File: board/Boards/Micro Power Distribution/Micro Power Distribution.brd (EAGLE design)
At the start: 48.2 x 84.8 mm, 24 parts

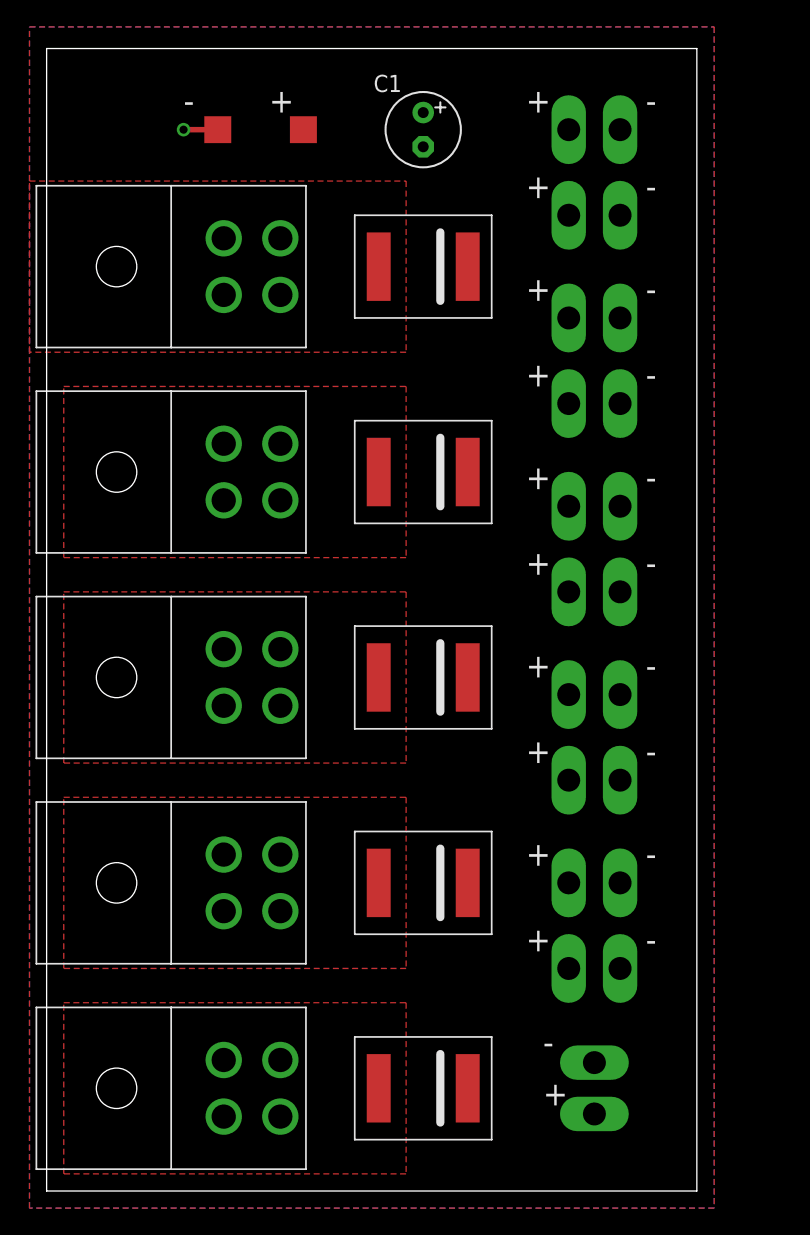
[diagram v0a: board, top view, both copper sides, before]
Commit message: updated power dist. board + created a micro version
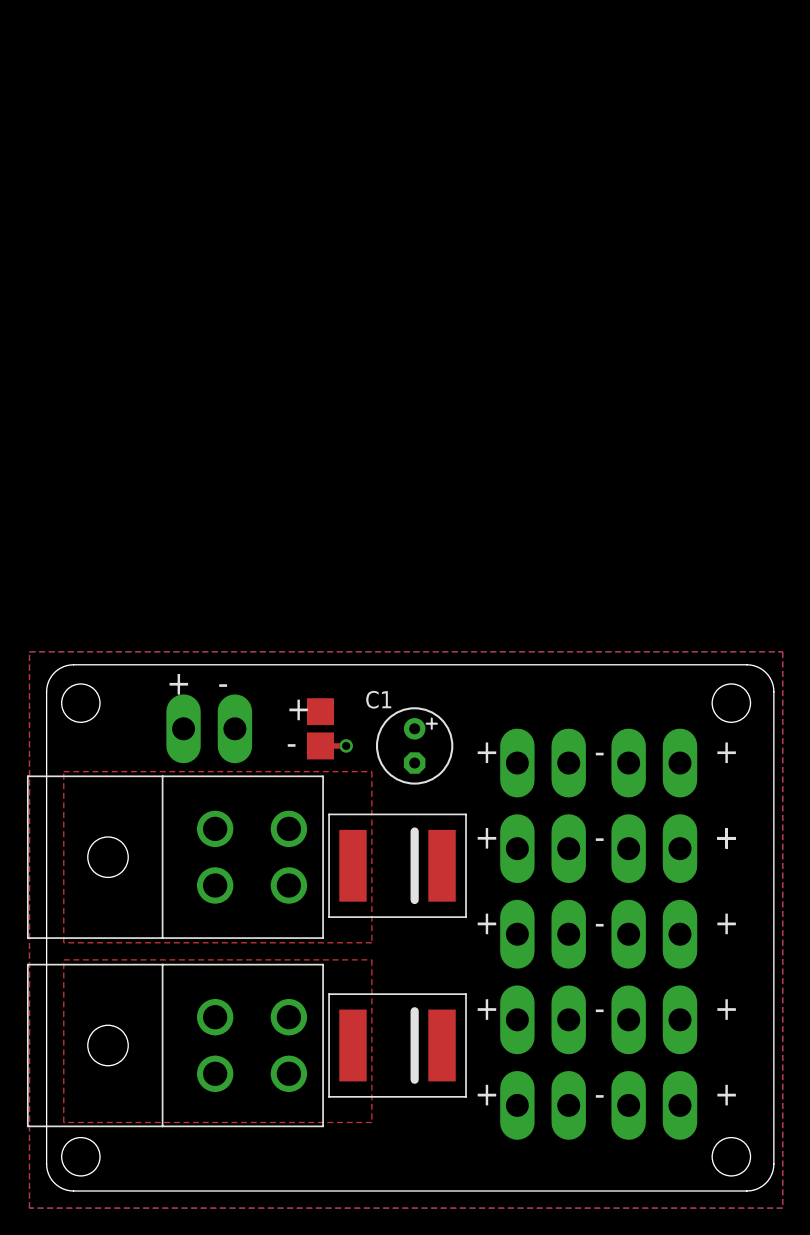
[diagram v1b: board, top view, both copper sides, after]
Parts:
- removed U$10, U$8, U$9: DO-214AB, Diodes:DO-214AB
- removed U$2, U$3, U$4: 2X2-MOLEX, Molex:2X2MOLEX
- moved TP4 53.5 mm to (45.1, 19.1), turned to 180 degrees
- moved TP8 47.2 mm to (45.1, 31.8), turned to 180 degrees
- moved TP13 46.4 mm to (20.3, 33.0)
- moved TP5 45.9 mm to (45.1, 12.7), turned to 180 degrees
- moved C1 45.7 mm to (27.3, 33.0)
- moved TP12 43.2 mm to (20.3, 35.6)
- moved TP6 38.4 mm to (45.1, 6.35), turned to 180 degrees
- moved TP9 33.2 mm to (36.8, 31.8)
- moved TP11 28.7 mm to (12.1, 34.3)
- moved TP10 25.8 mm to (45.1, 25.4), turned to 180 degrees
- moved TP7 6.35 mm to (36.8, 25.4)
- moved TP2 5.39 mm to (36.8, 12.7)
- moved TP3 5.39 mm to (36.8, 19.1)
- moved TP1 4.02 mm to (36.8, 6.35), turned to 0 degrees
- moved U$6 3.70 mm to (26.0, 10.8)
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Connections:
- removed net N$3: U$2.POWERL, U$2.POWERR, U$8.IN
- removed net N$4: U$3.POWERL, U$3.POWERR, U$9.IN
- removed net N$5: U$10.IN, U$4.POWERL, U$4.POWERR
- removed net N$6: C1.+, TP1.TP-1, TP10.TP-1, TP11.TP-1, TP12.TP, TP2.TP-1, TP3.TP-1, TP4.TP-1, TP5.TP-1, TP6.TP-1, TP7.TP-1, TP8.TP-1, TP9.TP-1, U$10.OUT, U$6.OUT, U$7.OUT, U$8.OUT, U$9.OUT
- new net N$10: C1.+, TP1.TP-1, TP10.TP-1, TP11.TP-1, TP12.TP, TP2.TP-1, TP3.TP-1, TP4.TP-1, TP5.TP-1, TP6.TP-1, TP7.TP-1, TP8.TP-1, TP9.TP-1, U$6.OUT, U$7.OUT
- net GND: no longer U$2.GNDL, U$2.GNDR, U$3.GNDL, U$3.GNDR, U$4.GNDL, U$4.GNDR
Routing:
- net GND: track 2.54 -> 1.91 mm
- added copper zone on layer 1, net N$10
- removed copper zone on layer 1, net N$3
- removed copper zone on layer 1, net N$4
- removed copper zone on layer 1, net N$5
- removed copper zone on layer 1, net N$6
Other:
- board size 48.2 x 84.8 mm -> 54 x 39 mm
- board text added: "hitchBOT micro Power Distribution Board C.G & D.K & R.E & D.B v1.0 - June 2015"
